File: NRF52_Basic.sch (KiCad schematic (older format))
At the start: 18 parts, among them J1 Conn_01x05_Male, J2 Conn_01x05_Male, J3 Conn_01x04_Male, J4 Conn_Coaxial, U1 nRF52832-QFxx, Y1 Crystal, Y2 Crystal

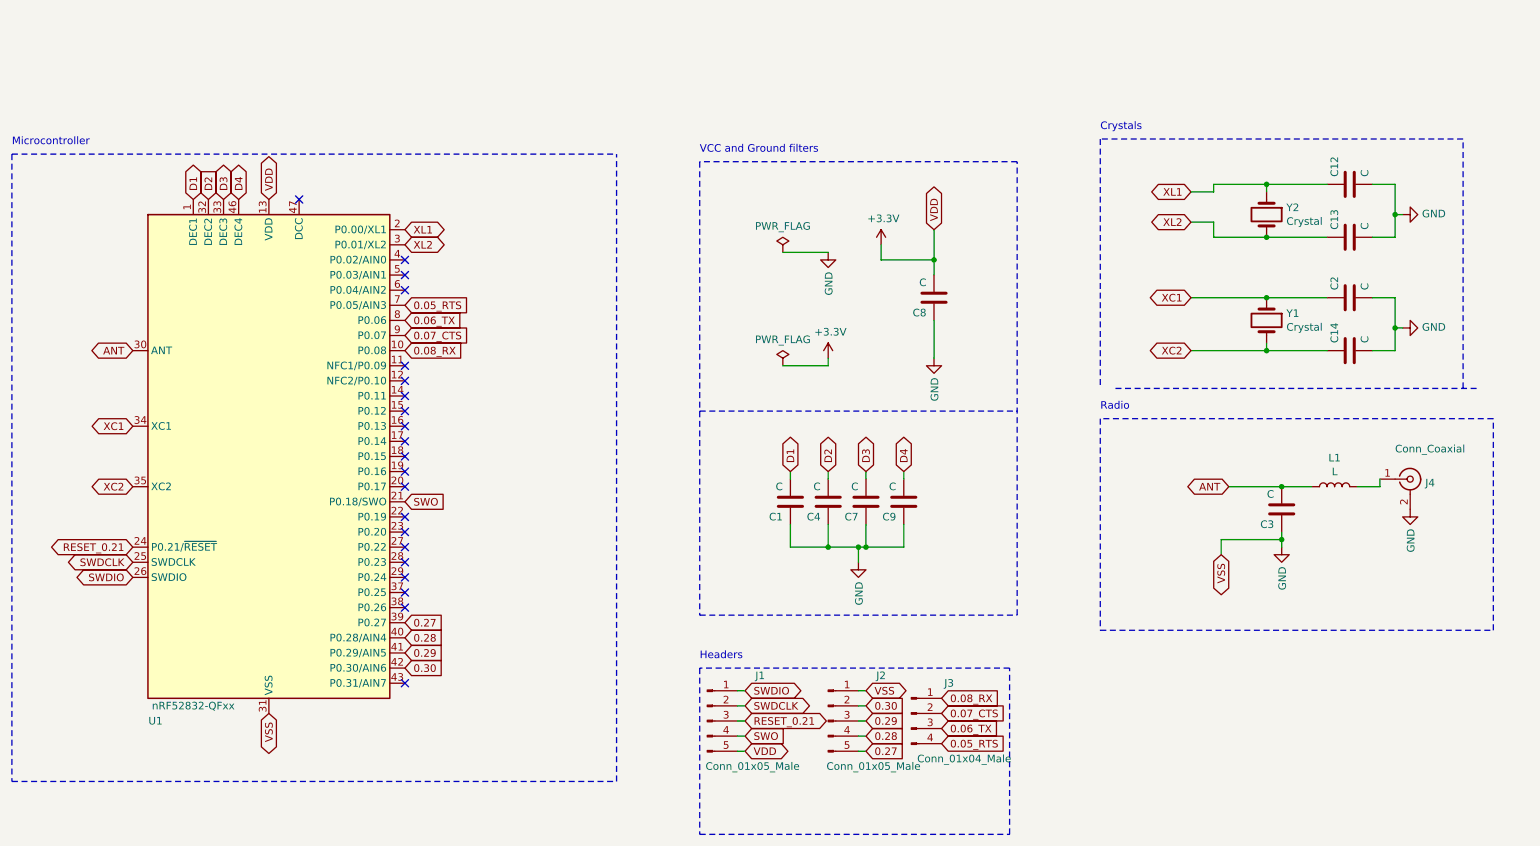
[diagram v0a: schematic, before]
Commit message: Improved ground fills and structure
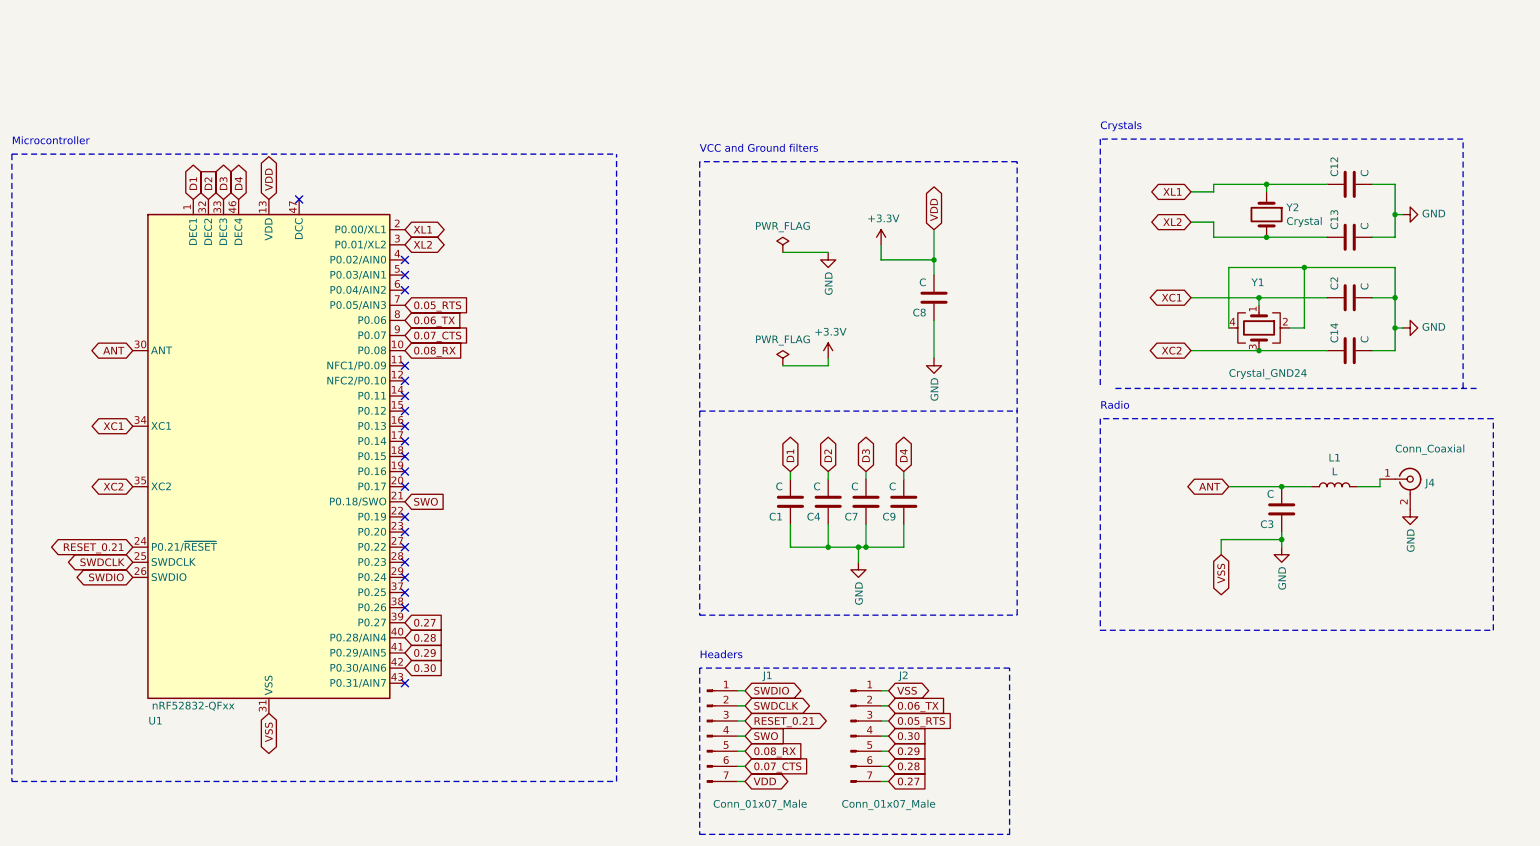
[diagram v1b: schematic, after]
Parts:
- removed J1, J2: Conn_01x05_Male, Connector_PinHeader_2.54mm:PinHeader_1x05_P2.54mm_Horizontal, symbol Connector:Conn_01x05_Male
- removed J3: Conn_01x04_Male, Connector_PinHeader_2.54mm:PinHeader_1x04_P2.54mm_Horizontal, symbol Connector:Conn_01x04_Male
- removed Y1: Crystal, Crystal:Crystal_SMD_2016-4Pin_2.0x1.6mm, symbol Device:Crystal
- added J1, J2: Conn_01x07_Male, Connector_PinSocket_2.54mm:PinSocket_1x07_P2.54mm_Vertical, symbol Connector:Conn_01x07_Male
- added Y1: Crystal_GND24, Crystal:Crystal_SMD_3225-4Pin_3.2x2.5mm, symbol Device:Crystal_GND24
- J4: footprint Connector_Coaxial:U.FL_Hirose_U.FL-R-SMT-1_Vertical -> Connector_Coaxial:SMA_Samtec_SMA-J-P-H-ST-EM1_EdgeMount
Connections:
- net +3V3: now also J1.7 (Pin_7)
- net 0.05_RTS: now also J2.3 (Pin_3)
- net 0.06_TX: now also J2.2 (Pin_2)
- net 0.07_CTS: now also J1.6 (Pin_6)
- net 0.08_RX: now also J1.5 (Pin_5)
- net 0.27: now also J2.7 (Pin_7)
- net 0.28: now also J2.6 (Pin_6)
- net 0.29: now also J2.5 (Pin_5)
- net 0.30: now also J2.4 (Pin_4)
- net GND: now also J2.1 (Pin_1), Y1.2, Y1.4
- net RESET_0.21: now also J1.3 (Pin_3)
- net SWDCLK: now also J1.2 (Pin_2)
- net SWDIO: now also J1.1 (Pin_1)
- net SWO: now also J1.4 (Pin_4)
- net XC1: now also Y1.1
- net XC2: now also Y1.3
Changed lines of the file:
@@
 	6100 5400 6050 5400
 Wire Wire Line
-	6850 5400 6900 5400
-Wire Wire Line
-	6850 5500 6900 5500
-Wire Wire Line
-	6850 5600 6900 5600
-Wire Wire Line
-	6850 5700 6900 5700
+	7000 5500 7050 5500
+Wire Wire Line
+	7000 5600 7050 5600
+Wire Wire Line
+	7000 5700 7050 5700
+Wire Wire Line
+	7000 5800 7050 5800
 Wire Notes Line
 	1250 5900 5250 5900
@@
 Text Notes 5800 5100 0    50   ~ 0
 Headers\n
-Text GLabel 6900 5300 2    50   BiDi ~ 0
+Text GLabel 7050 5300 2    50   BiDi ~ 0
 VSS
-Text GLabel 6100 5700 2    50   BiDi ~ 0
+Text GLabel 6100 5900 2    50   BiDi ~ 0
 VDD
 Wire Wire Line
 	6100 5300 6050 5300
 Wire Wire Line
-	6900 5300 6850 5300
+	7050 5400 7000 5400
 Wire Notes Line
 	5800 3450 7900 3450
@@
 Text GLabel 3850 4050 2    50   Input ~ 0
 SWO
-Text GLabel 7400 5450 2    50   Input ~ 0
-0.07_CTS
-Text GLabel 7400 5350 2    50   Input ~ 0
-0.08_RX
-Text GLabel 7400 5650 2    50   Input ~ 0
+Text GLabel 7050 5500 2    50   Input ~ 0
 0.05_RTS
 Text GLabel 3850 4950 2    50   Input ~ 0
@@
 Text GLabel 3850 5150 2    50   Input ~ 0
 0.30
-Text GLabel 6900 5600 2    50   Input ~ 0
+Text GLabel 7050 5800 2    50   Input ~ 0
 0.28
-Text GLabel 6900 5500 2    50   Input ~ 0
+Text GLabel 7050 5700 2    50   Input ~ 0
 0.29
-Text GLabel 6900 5400 2    50   Input ~ 0
+Text GLabel 7050 5600 2    50   Input ~ 0
 0.30
-Text GLabel 7400 5550 2    50   Input ~ 0
+Text GLabel 7050 5400 2    50   Input ~ 0
 0.06_TX
 Text GLabel 6100 5600 2    50   Input ~ 0
@@
 Text GLabel 3850 4850 2    50   Input ~ 0
 0.27
-Text GLabel 6900 5700 2    50   Input ~ 0
+Text GLabel 7050 5900 2    50   Input ~ 0
 0.27
 NoConn ~ 3850 3150
@@
 	10300 3950 10150 3950
 Wire Wire Line
-	9050 2700 9550 2700
-Wire Wire Line
 	10400 2700 10400 2900
-Wire Wire Line
-	9050 3050 9550 3050
-$Comp
-L Device:Crystal Y1
-U 1 1 6043DEA4
-P 9550 2850
-F 0 "Y1" V 9504 2981 50  0000 L CNN
-F 1 "Crystal" V 9595 2981 50  0000 L CNN
-F 2 "Crystal:Crystal_SMD_2016-4Pin_2.0x1.6mm" H 9550 2850 50  0001 C CNN
-F 3 "~" H 9550 2850 50  0001 C CNN
-	1    9550 2850
-	0    1    1    0
-$EndComp
-Connection ~ 9550 2700
-Wire Wire Line
-	9550 3000 9550 3050
-Connection ~ 9550 3050
-Wire Wire Line
-	9550 2700 9950 2700
-Wire Wire Line
-	9550 3050 9950 3050
 Text GLabel 3850 2950 2    50   Input ~ 0
 0.07_CTS
@@
 	5250 5900 5250 1750
 $Comp
-L Connector:Conn_01x05_Male J2
-U 1 1 602A1200
-P 6650 5500
-F 0 "J2" H 7000 5800 50  0000 C CNN
-F 1 "Conn_01x05_Male" H 6950 5200 50  0000 C CNN
-F 2 "Connector_PinHeader_2.54mm:PinHeader_1x05_P2.54mm_Horizontal" H 6650 5500 50  0001 C CNN
-F 3 "~" H 6650 5500 50  0001 C CNN
-	1    6650 5500
-	1    0    0    -1
-$EndComp
-$Comp
-L Connector:Conn_01x04_Male J3
-U 1 1 602A279D
-P 7200 5450
-F 0 "J3" H 7450 5650 50  0000 C CNN
-F 1 "Conn_01x04_Male" H 7550 5150 50  0000 C CNN
-F 2 "Connector_PinHeader_2.54mm:PinHeader_1x04_P2.54mm_Horizontal" H 7200 5450 50  0001 C CNN
-F 3 "~" H 7200 5450 50  0001 C CNN
-	1    7200 5450
-	1    0    0    -1
-$EndComp
-$Comp
-L Connector:Conn_01x05_Male J1
-U 1 1 602A8D09
-P 5850 5500
-F 0 "J1" H 6200 5800 50  0000 C CNN
-F 1 "Conn_01x05_Male" H 6150 5200 50  0000 C CNN
-F 2 "Connector_PinHeader_2.54mm:PinHeader_1x05_P2.54mm_Horizontal" H 5850 5500 50  0001 C CNN
-F 3 "~" H 5850 5500 50  0001 C CNN
-	1    5850 5500
-	1    0    0    -1
-$EndComp
-$Comp
 L Connector:Conn_Coaxial J4
 U 1 1 602E44FD
@@
 F 0 "J4" H 10600 3875 50  0000 L CNN
 F 1 "Conn_Coaxial" H 10400 4100 50  0000 L CNN
-F 2 "Connector_Coaxial:U.FL_Hirose_U.FL-R-SMT-1_Vertical" H 10500 3900 50  0001 C CNN
+F 2 "Connector_Coaxial:SMA_Samtec_SMA-J-P-H-ST-EM1_EdgeMount" H 10500 3900 50  0001 C CNN
 F 3 " ~" H 10500 3900 50  0001 C CNN
 	1    10500 3900
@@
 NoConn ~ 3850 5250
 NoConn ~ 3850 2650
+Text GLabel 6100 5800 2    50   Input ~ 0
+0.07_CTS
+Text GLabel 6100 5700 2    50   Input ~ 0
+0.08_RX
+$Comp
+L Connector:Conn_01x07_Male J2
+U 1 1 602D748A
+P 6800 5600
+F 0 "J2" H 7150 6000 50  0000 C CNN
+F 1 "Conn_01x07_Male" H 7050 5150 50  0000 C CNN
+F 2 "Connector_PinSocket_2.54mm:PinSocket_1x07_P2.54mm_Vertical" H 6800 5600 50  0001 C CNN
+F 3 "~" H 6800 5600 50  0001 C CNN
+	1    6800 5600
+	1    0    0    -1
+$EndComp
+$Comp
+L Connector:Conn_01x07_Male J1
+U 1 1 602D8565
+P 5850 5600
+F 0 "J1" H 6250 6000 50  0000 C CNN
+F 1 "Conn_01x07_Male" H 6200 5150 50  0000 C CNN
+F 2 "Connector_PinSocket_2.54mm:PinSocket_1x07_P2.54mm_Vertical" H 5850 5600 50  0001 C CNN
+F 3 "~" H 5850 5600 50  0001 C CNN
+	1    5850 5600
+	1    0    0    -1
+$EndComp
+Wire Wire Line
+	6050 5800 6100 5800
+Wire Wire Line
+	6050 5900 6100 5900
+Wire Wire Line
+	7000 5900 7050 5900
+Wire Wire Line
+	7000 5300 7050 5300
+$Comp
+L Device:Crystal_GND24 Y1
+U 1 1 602F2598
+P 9500 2900
+F 0 "Y1" V 9200 2850 50  0000 L CNN
+F 1 "Crystal_GND24" V 9800 2700 50  0000 L CNN
+F 2 "Crystal:Crystal_SMD_3225-4Pin_3.2x2.5mm" H 9500 2900 50  0001 C CNN
+F 3 "~" H 9500 2900 50  0001 C CNN
+	1    9500 2900
+	0    1    1    0
+$EndComp
+Wire Wire Line
+	9050 2700 9500 2700
+Wire Wire Line
+	9500 2750 9500 2700
+Connection ~ 9500 2700
+Wire Wire Line
+	9500 2700 9950 2700
+Wire Wire Line
+	9050 3050 9500 3050
+Connection ~ 9500 3050
+Wire Wire Line
+	9500 3050 9950 3050
+Wire Wire Line
+	9300 2900 9300 2500
+Wire Wire Line
+	9300 2500 9800 2500
+Wire Wire Line
+	10400 2500 10400 2700
+Connection ~ 10400 2700
+Wire Wire Line
+	9700 2900 9800 2900
+Wire Wire Line
+	9800 2900 9800 2500
+Connection ~ 9800 2500
+Wire Wire Line
+	9800 2500 10400 2500
 $EndSCHEMATC

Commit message: Intermediate mods -2
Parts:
- C1: value C -> 100nF; LCSC Part # (none) -> C14663
- C12, C13, C14, C2: value C -> 12pF; LCSC Part # (none) -> C38523
- C3: value C -> 0.8pF; LCSC Part # (none) -> C21357
- C4, C7: value C -> 100pF; LCSC Part # (none) -> C14858
- C8: value C -> 4.7uF; LCSC Part # (none) -> C19666
- C9: value C -> 1.0uF; LCSC Part # (none) -> C52923
- L1: value L -> 3.9nH; LCSC Part # (none) -> C13818
- U1: LCSC Part # (none) -> C77540
- Y1: LCSC Part # (none) -> C91742
- Y2: LCSC Part # (none) -> C280831
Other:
- note added: "Values and circuitry copied from:"
- note added: "https://infocenter.nordicsemi.com/index.jsp?topic=%2Fcom.nordic.infocenter.nrf52832.ps.v1.1%2Fref_circuitry.html"
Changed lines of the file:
@@
 P 6650 4050
 F 0 "C4" H 6700 4150 50  0000 L CNN
-F 1 "C" H 6700 3950 50  0000 L CNN
+F 1 "100pF" H 6700 3950 50  0000 L CNN
 F 2 "Capacitor_SMD:C_0201_0603Metric" H 6688 3900 50  0001 C CNN
 F 3 "~" H 6650 4050 50  0001 C CNN
+F 4 "C14858" H 6650 4050 50  0001 C CNN "LCSC Part #"
 	1    6650 4050
 	-1   0    0    1
@@
 P 6400 4050
 F 0 "C1" H 6450 4150 50  0000 L CNN
-F 1 "C" H 6450 3950 50  0000 L CNN
+F 1 "100nF" H 6450 3950 50  0000 L CNN
 F 2 "Capacitor_SMD:C_0201_0603Metric" H 6438 3900 50  0001 C CNN
 F 3 "~" H 6400 4050 50  0001 C CNN
+F 4 "C14663" H 6400 4050 50  0001 C CNN "LCSC Part #"
 	1    6400 4050
 	-1   0    0    1
@@
 P 6900 4050
 F 0 "C7" H 6950 4150 50  0000 L CNN
-F 1 "C" H 6950 3950 50  0000 L CNN
+F 1 "100pF" H 6950 3950 50  0000 L CNN
 F 2 "Capacitor_SMD:C_0201_0603Metric" H 6938 3900 50  0001 C CNN
 F 3 "~" H 6900 4050 50  0001 C CNN
+F 4 "C14858" H 6900 4050 50  0001 C CNN "LCSC Part #"
 	1    6900 4050
 	-1   0    0    1
@@
 P 7150 4050
 F 0 "C9" H 7200 4150 50  0000 L CNN
-F 1 "C" H 7200 3950 50  0000 L CNN
+F 1 "1.0uF" H 7200 3950 50  0000 L CNN
 F 2 "Capacitor_SMD:C_0402_1005Metric" H 7188 3900 50  0001 C CNN
 F 3 "~" H 7150 4050 50  0001 C CNN
+F 4 "C52923" H 7150 4050 50  0001 C CNN "LCSC Part #"
 	1    7150 4050
 	-1   0    0    1
@@
 P 7350 2700
 F 0 "C8" H 7400 2800 50  0000 L CNN
-F 1 "C" H 7400 2600 50  0000 L CNN
+F 1 "4.7uF" H 7400 2600 50  0000 L CNN
 F 2 "Capacitor_SMD:C_0603_1608Metric" H 7388 2550 50  0001 C CNN
 F 3 "~" H 7350 2700 50  0001 C CNN
+F 4 "C19666" H 7350 2700 50  0001 C CNN "LCSC Part #"
 	1    7350 2700
 	-1   0    0    1
@@
 P 9650 4100
 F 0 "C3" H 9700 4200 50  0000 L CNN
-F 1 "C" H 9700 4000 50  0000 L CNN
+F 1 "0.8pF" H 9700 4000 50  0000 L CNN
 F 2 "Capacitor_SMD:C_0201_0603Metric" H 9688 3950 50  0001 C CNN
 F 3 "~" H 9650 4100 50  0001 C CNN
+F 4 "C21357" H 9650 4100 50  0001 C CNN "LCSC Part #"
 	1    9650 4100
 	-1   0    0    1
@@
 P 10000 3950
 F 0 "L1" V 10190 3950 50  0000 C CNN
-F 1 "L" V 10099 3950 50  0000 C CNN
+F 1 "3.9nH" V 10099 3950 50  0000 C CNN
 F 2 "Inductor_SMD:L_0201_0603Metric" H 10000 3950 50  0001 C CNN
 F 3 "~" H 10000 3950 50  0001 C CNN
+F 4 "C13818" H 10000 3950 50  0001 C CNN "LCSC Part #"
 	1    10000 3950
 	0    -1   -1   0
@@
 P 10100 1950
 F 0 "C12" H 10150 2050 50  0000 L CNN
-F 1 "C" H 10150 1850 50  0000 L CNN
+F 1 "12pF" H 10150 1850 50  0000 L CNN
 F 2 "Capacitor_SMD:C_0201_0603Metric" H 10138 1800 50  0001 C CNN
 F 3 "~" H 10100 1950 50  0001 C CNN
+F 4 "C38523" H 10100 1950 50  0001 C CNN "LCSC Part #"
 	1    10100 1950
 	0    -1   -1   0
@@
 P 10100 2300
 F 0 "C13" H 10150 2400 50  0000 L CNN
-F 1 "C" H 10150 2200 50  0000 L CNN
+F 1 "12pF" H 10150 2200 50  0000 L CNN
 F 2 "Capacitor_SMD:C_0201_0603Metric" H 10138 2150 50  0001 C CNN
 F 3 "~" H 10100 2300 50  0001 C CNN
+F 4 "C38523" H 10100 2300 50  0001 C CNN "LCSC Part #"
 	1    10100 2300
 	0    -1   -1   0
@@
 F 2 "Crystal:Crystal_SMD_2012-2Pin_2.0x1.2mm" H 9550 2150 50  0001 C CNN
 F 3 "~" H 9550 2150 50  0001 C CNN
+F 4 "C280831" H 9550 2150 50  0001 C CNN "LCSC Part #"
 	1    9550 2150
 	0    1    1    0
@@
 P 10100 2700
 F 0 "C2" H 10150 2800 50  0000 L CNN
-F 1 "C" H 10150 2600 50  0000 L CNN
+F 1 "12pF" H 10150 2600 50  0000 L CNN
 F 2 "Capacitor_SMD:C_0201_0603Metric" H 10138 2550 50  0001 C CNN
 F 3 "~" H 10100 2700 50  0001 C CNN
+F 4 "C38523" H 10100 2700 50  0001 C CNN "LCSC Part #"
 	1    10100 2700
 	0    -1   -1   0
@@
 P 10100 3050
 F 0 "C14" H 10150 3150 50  0000 L CNN
-F 1 "C" H 10150 2950 50  0000 L CNN
+F 1 "12pF" H 10150 2950 50  0000 L CNN
 F 2 "Capacitor_SMD:C_0201_0603Metric" H 10138 2900 50  0001 C CNN
 F 3 "~" H 10100 3050 50  0001 C CNN
+F 4 "C38523" H 10100 3050 50  0001 C CNN "LCSC Part #"
 	1    10100 3050
 	0    -1   -1   0
@@
 F 2 "Package_DFN_QFN:QFN-48-1EP_6x6mm_P0.4mm_EP4.6x4.6mm" H 2950 1650 50  0001 C CNN
 F 3 "http://infocenter.nordicsemi.com/pdf/nRF52832_PS_v1.4.pdf" H 2450 3950 50  0001 C CNN
+F 4 "C77540" H 2950 3750 50  0001 C CNN "LCSC Part #"
 	1    2950 3750
 	1    0    0    -1
@@
 F 2 "Crystal:Crystal_SMD_3225-4Pin_3.2x2.5mm" H 9500 2900 50  0001 C CNN
 F 3 "~" H 9500 2900 50  0001 C CNN
+F 4 "C91742" H 9500 2900 50  0001 C CNN "LCSC Part #"
 	1    9500 2900
 	0    1    1    0
@@
 Wire Wire Line
 	9800 2500 10400 2500
+Text Notes 5850 1300 0    50   ~ 0
+https://infocenter.nordicsemi.com/index.jsp?topic=%2Fcom.nordic.infocenter.nrf52832.ps.v1.1%2Fref_circuitry.html
+Text Notes 5850 1100 0    50   ~ 0
+Values and circuitry copied from:
 $EndSCHEMATC
